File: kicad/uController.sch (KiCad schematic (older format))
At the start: 62 parts, among them SW1 Edit, SW2 Up, SW3 Dw, U1 LM2575-5.0BT, U2 DS1307

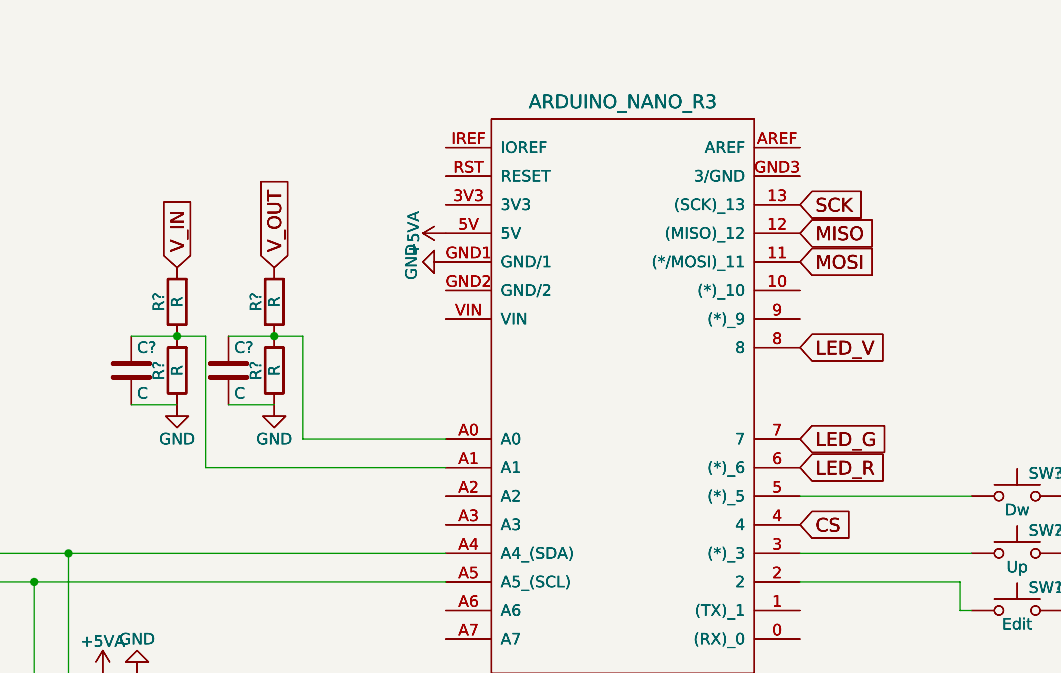
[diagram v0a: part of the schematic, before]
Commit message: Schematical hierarchical structure enhanced
Work on schematical page KiCad
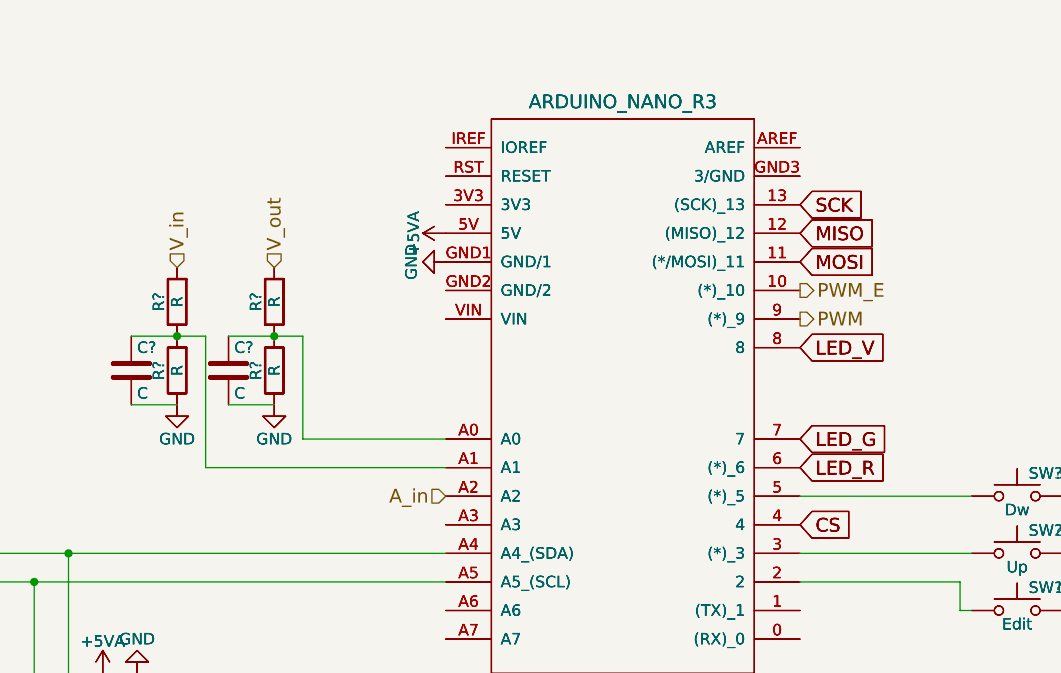
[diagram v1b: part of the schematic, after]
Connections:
- net PWM_E: now reaches SH?.10 ((*)_10), SH?.10 ((*)_10)
- net PWM: now reaches SH?.9 ((*)_9), SH?.9 ((*)_9)
- net A_in: now reaches SH?.A2, SH?.A2
- net V_IN renamed V_in
- net V_OUT renamed V_out
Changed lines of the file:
@@
 	1    0    0    -1
 $EndComp
-Text GLabel 4675 2600 1    60   Input ~ 0
-V_IN
-Text GLabel 5100 2600 1    60   Input ~ 0
-V_OUT
 Text GLabel 2150 6575 0    60   Input ~ 0
 v_IN
@@
 	1    0    0    -1
 $EndComp
-Text GLabel 4675 2600 1    60   Input ~ 0
-V_IN
-Text GLabel 5100 2600 1    60   Input ~ 0
-V_OUT
 Text GLabel 2150 6575 0    60   Input ~ 0
 v_IN
@@
 	0    1    1    0
 $EndComp
+Text HLabel 4675 2600 1    60   Input ~ 0
+V_in
+Text HLabel 5100 2600 1    60   Input ~ 0
+V_out
+Text HLabel 5850 3600 0    60   Input ~ 0
+A_in
+Text HLabel 7400 2825 2    60   Output ~ 0
+PWM
+Text HLabel 7400 2700 2    60   Output ~ 0
+PWM_E
 $EndSCHEMATC

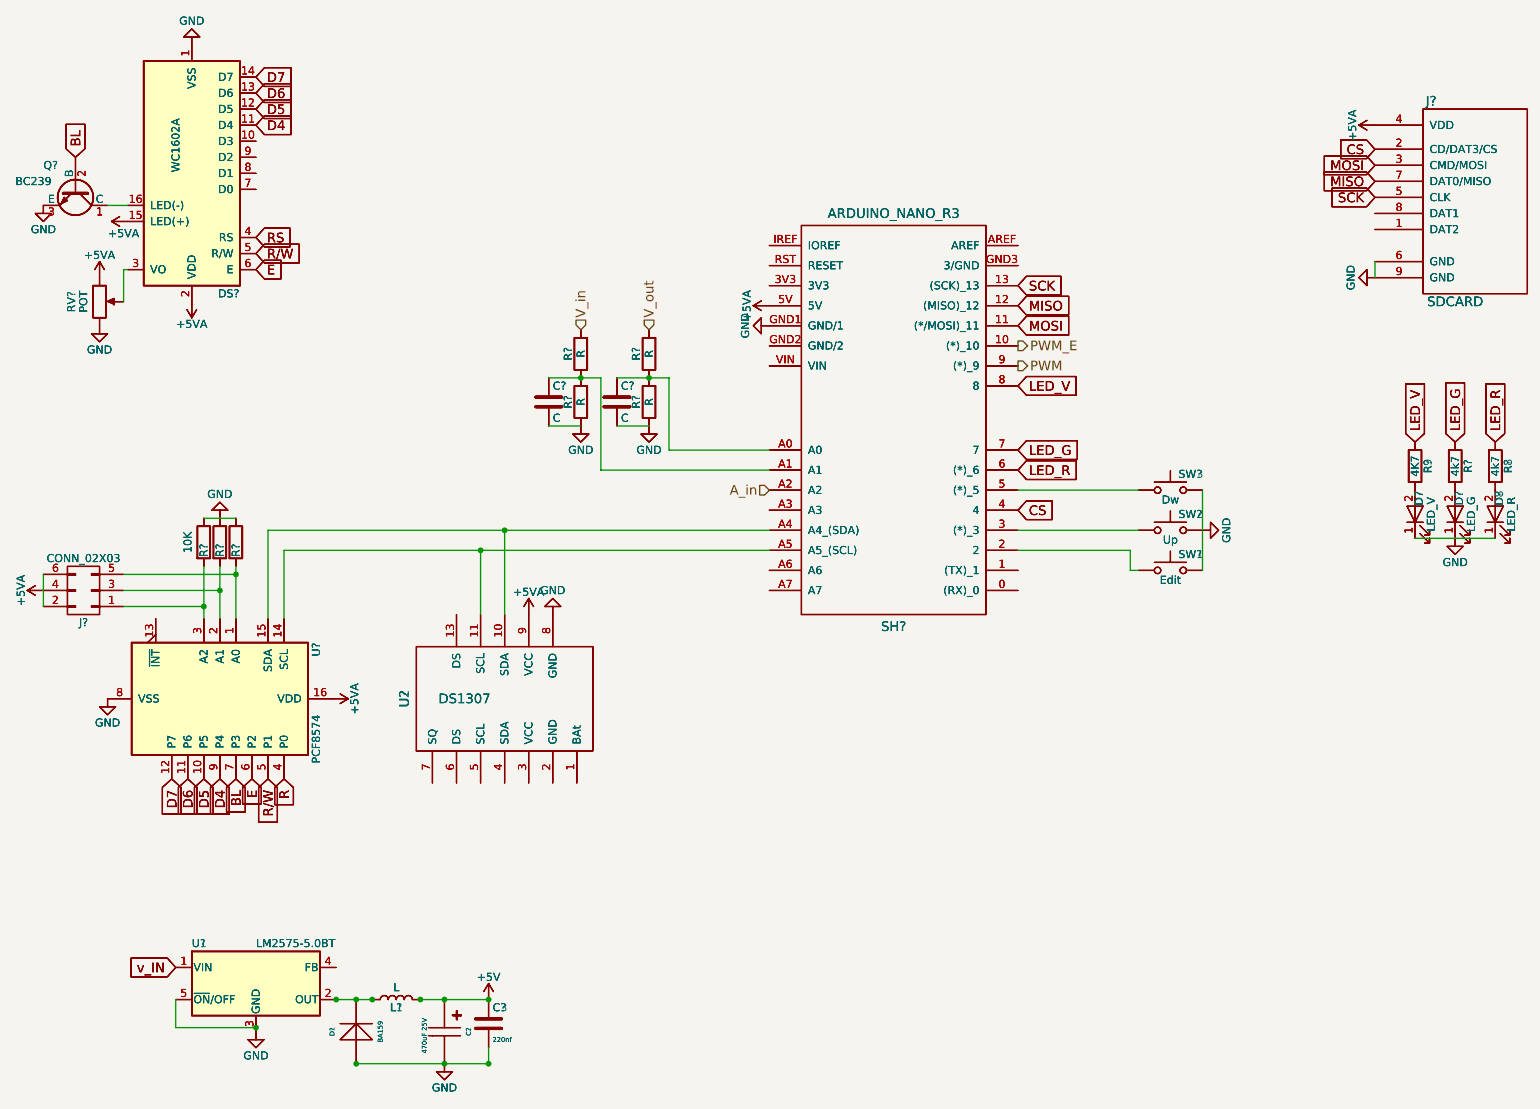
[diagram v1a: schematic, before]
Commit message: Build hierarchy schematic
From the first schematic split in two page uController and Power
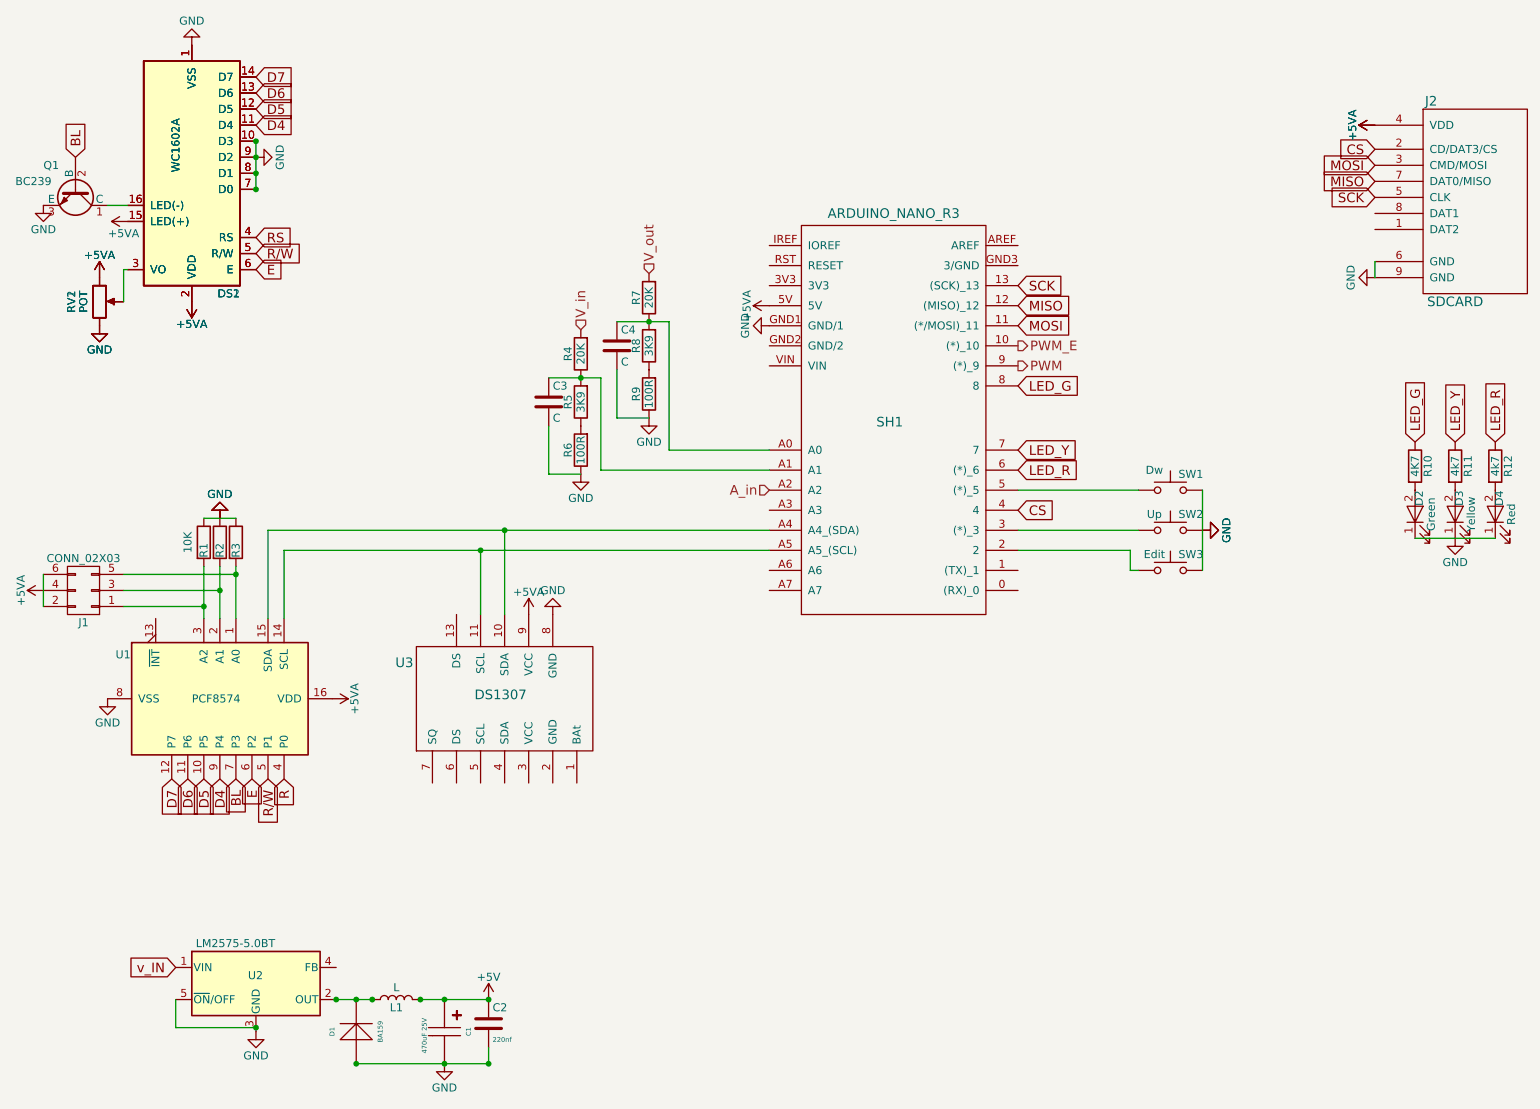
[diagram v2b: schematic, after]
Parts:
- removed C2: 470uF 25V, symbol CAPACITOR_POLARISED_RevE_Date15jun2010
- removed C3: 220nf, symbol C
- removed C? (x2): C, symbol C
- removed D1: BA159, symbol DIODE-STANDARD_RevE_Date15jun2010
- removed D7: LED_V, symbol LED
- removed D8: LED_R, symbol LED
- removed D?: LED_G, symbol LED
- removed J?: CONN_02X03, symbol CONN_02X03
- removed J?: SDCARD, symbol SDCARD
- removed L1: L, symbol L
- removed Q?: BC239, TO_SOT_Packages_THT:TO-92_Molded_Narrow, symbol BC237
- removed R8, R?: 4k7, symbol R
- removed R?: 10K, symbol R
- removed R? (x6): R, symbol R
- removed SH?: ARDUINO_NANO_R3, symbol ARDUINO_NANO_R3
- removed SW1: Edit, symbol SW_Push
- removed SW2: Up, symbol SW_Push
- removed SW3: Dw, symbol SW_Push
- removed U1: LM2575-5.0BT, TO_SOT_Packages_THT:TO-220-5_Vertical, symbol LM2575-5.0BT
- removed U2: DS1307, symbol DS1307
- removed U?: PCF8574, symbol PCF8574
- added R6: 100R, symbol R
- D2: renamed from D?; value LED_V -> Green
- D3: renamed from D?; value LED_G -> Yellow
- D4: renamed from D?; value LED_R -> Red
- R4, R7: renamed from R?; value R -> 20K
- R5, R8: renamed from R?; value R -> 3K9
- R9: value 4K7 -> 100R
- gave numbers to parts that had none: 26
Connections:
- net GND: now also DS1.10 (D3), DS1.7 (D0), DS1.8 (D1), DS1.9 (D2), DS2.10 (D3), DS2.7 (D0), DS2.8 (D1), DS2.9 (D2), R9.1, R6.1; no longer R5.1, R8.1
- net LED_G: now also R10.1, SH1.8; no longer R11.1, SH1.7
- net at D2.2 (A), R10.2: no longer R9.2
- removed net LED_V: R10.1, R9.1, SH1.8
- new net: R5.1, R6.2
- new net: R8.1, R9.2
- new net LED_Y: R11.1, SH1.7
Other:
- moved on the sheet: C4, R7, R8
